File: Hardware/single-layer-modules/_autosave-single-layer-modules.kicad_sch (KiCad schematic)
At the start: 19 parts, among them J1 Blue Pill - 1, J2 Blue Pill - 2, J3 SIM800L, J4 DS18B20, J5 DHT11, J6 FC-28, J7 MQ-02, Q1 FDS9435A, Q2 2N3904, SW1 SW_DIP_x05

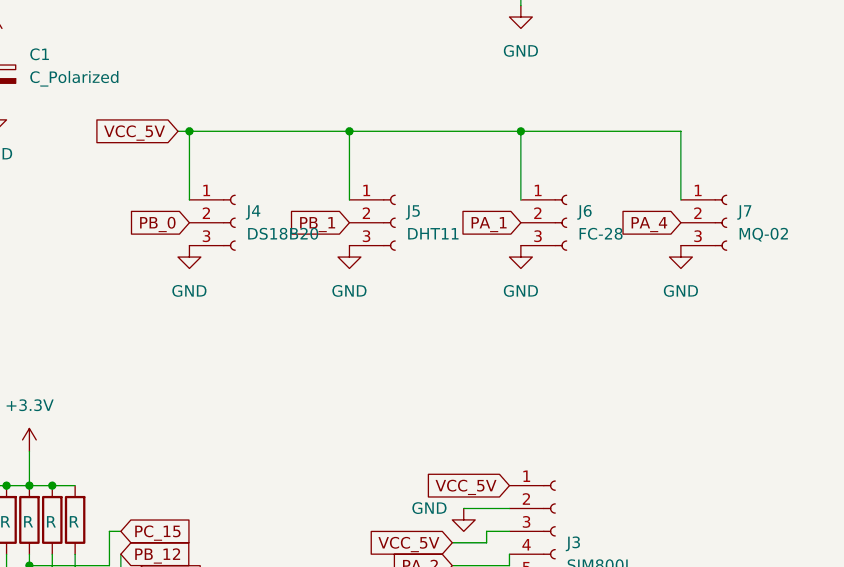
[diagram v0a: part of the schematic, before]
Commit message: Add autosave and backup files for PCB project
Added KiCad autosave and backup files for the single-layer-modules project, including .kicad_pcb, .kicad_sch, and backup zip archives. Updated main PCB and schematic files with recent changes. Lock files for autosave and schematic were also added.
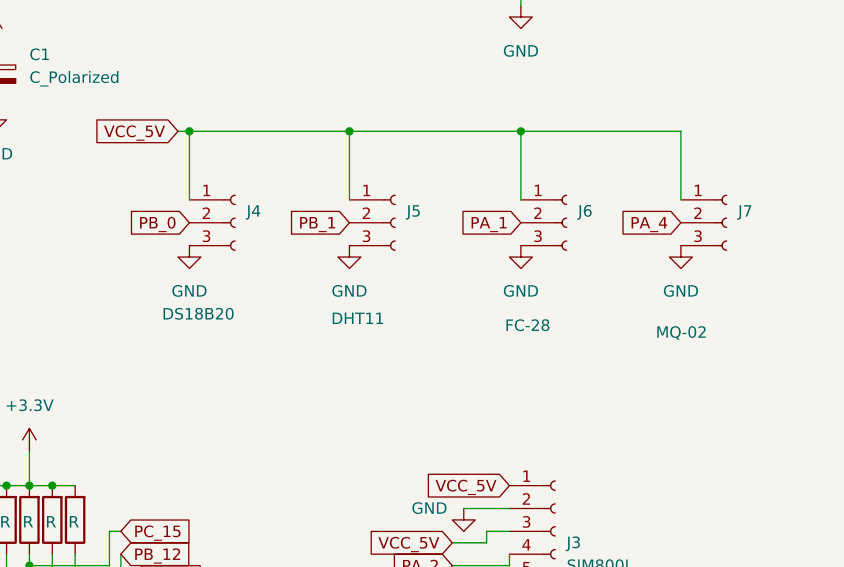
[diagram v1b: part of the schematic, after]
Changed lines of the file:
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@@
 		(on_board yes)
 		(dnp no)
-		(fields_autoplaced yes)
 		(property "Reference" "J5"
 			(at 187.96 73.6599 0)
@@
 		)
 		(property "Value" "DHT11"
-			(at 187.96 76.1999 0)
+			(at 179.578 85.598 0)
 			(effects
 				(font
@@
 		(on_board yes)
 		(dnp no)
-		(fields_autoplaced yes)
 		(property "Reference" "J7"
 			(at 224.79 73.6599 0)
@@
 		)
 		(property "Value" "MQ-02"
-			(at 224.79 76.1999 0)
+			(at 215.646 87.122 0)
 			(effects
 				(font
@@
 		)
 		(property "Value" "FC-28"
-			(at 207.01 76.1999 0)
+			(at 198.882 86.36 0)
 			(effects
 				(font
@@
 		(on_board yes)
 		(dnp no)
-		(fields_autoplaced yes)
 		(property "Reference" "J4"
 			(at 170.18 73.6599 0)
@@
 		)
 		(property "Value" "DS18B20"
-			(at 170.18 76.1999 0)
-			(effects
-				(font
+			(at 160.782 85.09 0)
+			(effects
+				(font
